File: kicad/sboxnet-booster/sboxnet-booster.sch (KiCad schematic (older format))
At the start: 53 parts, among them J1 sboxnet-stecker_02x17, J2 Conn_01x02_Male, J3 Conn_01x02_Male, J4 Conn_01x02_Male, J5 Screw_Terminal_01x04, J6 Screw_Terminal_01x04, J7 Power von externen 15V/4A Net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, SW1 Öffner, U1 l6206

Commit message: update booster kicad
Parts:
- removed C4: 220n, Capacitor_THT:C_Axial_L3.8mm_D2.6mm_P7.50mm_Horizontal, symbol Device:C
- removed J2: Conn_01x02_Male, Connector_PinHeader_2.54mm:PinHeader_1x02_P2.54mm_Vertical, symbol Connector:Conn_01x02_Male
- removed R13: 0.25 / 2W, Resistor_THT:R_Axial_DIN0414_L11.9mm_D4.5mm_P20.32mm_Horizontal, symbol Device:R
- removed R14, R15: 10k, Resistor_THT:R_Axial_DIN0204_L3.6mm_D1.6mm_P7.62mm_Horizontal, symbol Device:R
- removed U1: l6206, sboxnet:POWERSO36, symbol sboxnet:l6206
- added U1: L6206PSO, Package_SO:HSOP-36-1EP_11.0x15.9mm_P0.65mm_SlugDown_ThermalVias, symbol sboxnet:L6206PSO
- C1, C2, C3, C5, C6: footprint Capacitor_THT:C_Axial_L3.8mm_D2.6mm_P7.50mm_Horizontal -> Capacitor_SMD:C_1206_3216Metric
- C7: footprint Capacitor_THT:CP_Radial_D10.0mm_P2.50mm -> Capacitor_THT:CP_Radial_D12.5mm_P5.00mm
- C8: footprint Capacitor_THT:CP_Radial_D10.0mm_P2.50mm -> Capacitor_THT:CP_Radial_D5.0mm_P2.00mm
- R1, R10, R11, R2, R3, R4, R5, R6, R7, R8, R9: footprint Resistor_THT:R_Axial_DIN0204_L3.6mm_D1.6mm_P5.08mm_Horizontal -> Resistor_SMD:R_1206_3216Metric
- R12: value 0.25 / 2W -> 10k; footprint Resistor_THT:R_Axial_DIN0414_L11.9mm_D4.5mm_P20.32mm_Horizontal -> Resistor_SMD:R_1206_3216Metric
- R16, R17, R18, R19, R20: footprint Resistor_THT:R_Axial_DIN0204_L3.6mm_D1.6mm_P7.62mm_Horizontal -> Resistor_SMD:R_1206_3216Metric
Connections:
- net labels added: OUT1a, OUT1b, OUT2a, OUT2b, VBOOT, VCP
- net labels removed: SENSE
- wire segments 111 -> 86
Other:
- note removed: "Strommessung"

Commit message: fixed booster L6206PSO
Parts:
- J1: symbol sboxnet:sboxnet-stecker_02x17 -> sboxnet-booster-rescue:sboxnet-stecker_02x17-sboxnet
- U1: symbol sboxnet:L6206PSO -> sboxnet-booster-rescue:L6206PSO-sboxnet
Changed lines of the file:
@@
 	6485 3170 6530 3170
 $Comp
-L sboxnet:sboxnet-stecker_02x17 J1
+L sboxnet-booster-rescue:sboxnet-stecker_02x17-sboxnet J1
 U 1 1 5DC2D77D
 P 1200 3790
@@
 	730  3790 950  3790
 $Comp
-L sboxnet:L6206PSO U1
+L sboxnet-booster-rescue:L6206PSO-sboxnet U1
 U 1 1 5F0CD7F1
 P 5010 3755

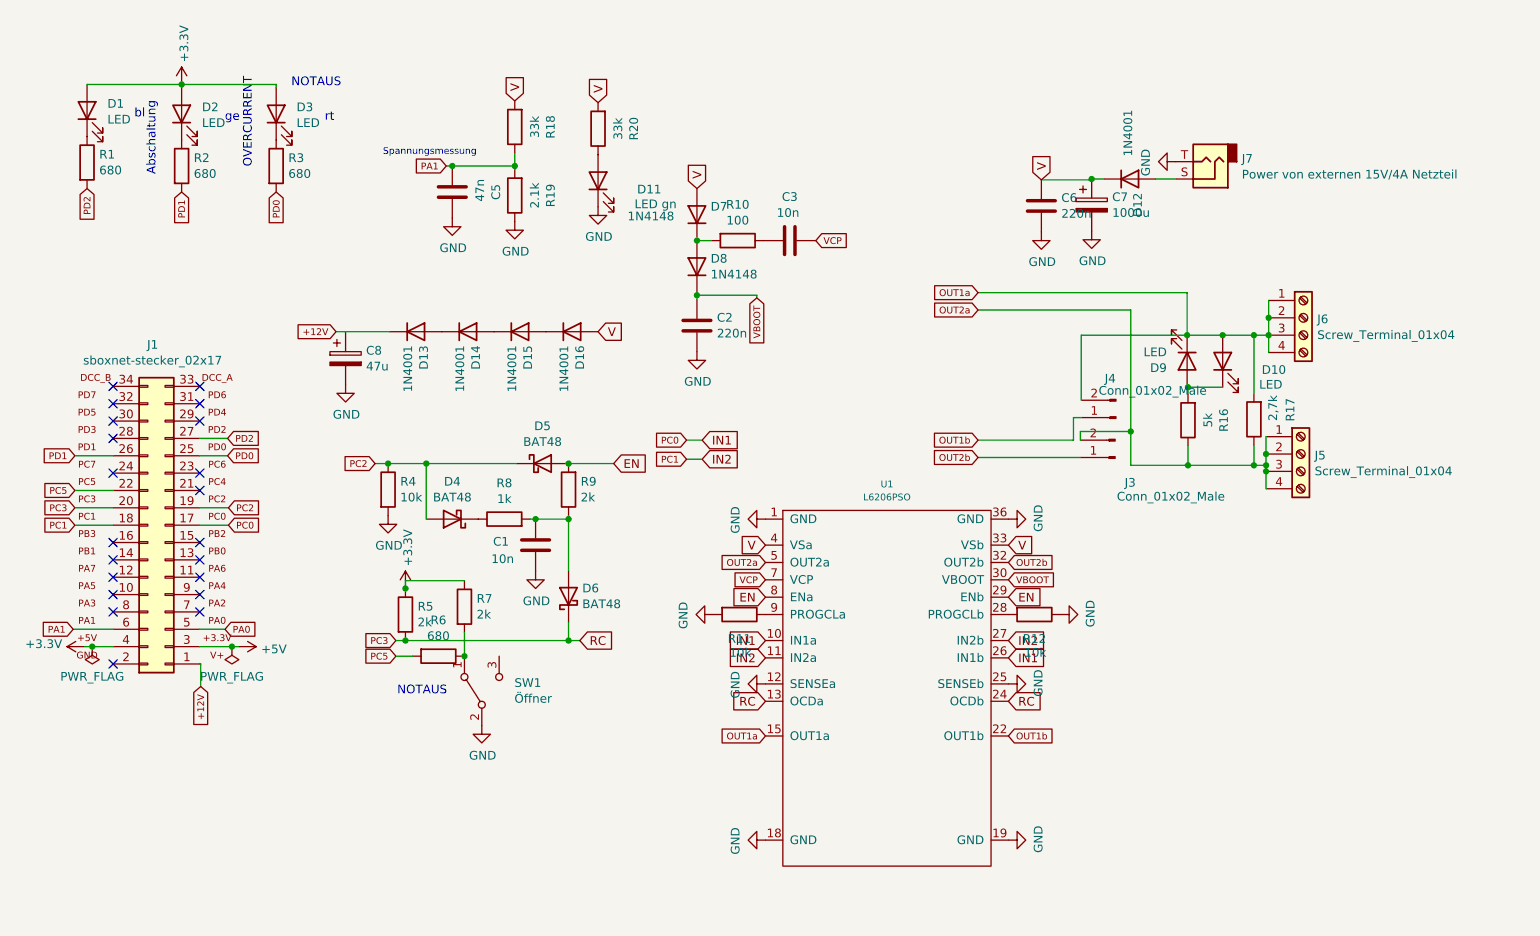
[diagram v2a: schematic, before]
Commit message: update booster layout with POWERSO Slug Down Terminal Vias
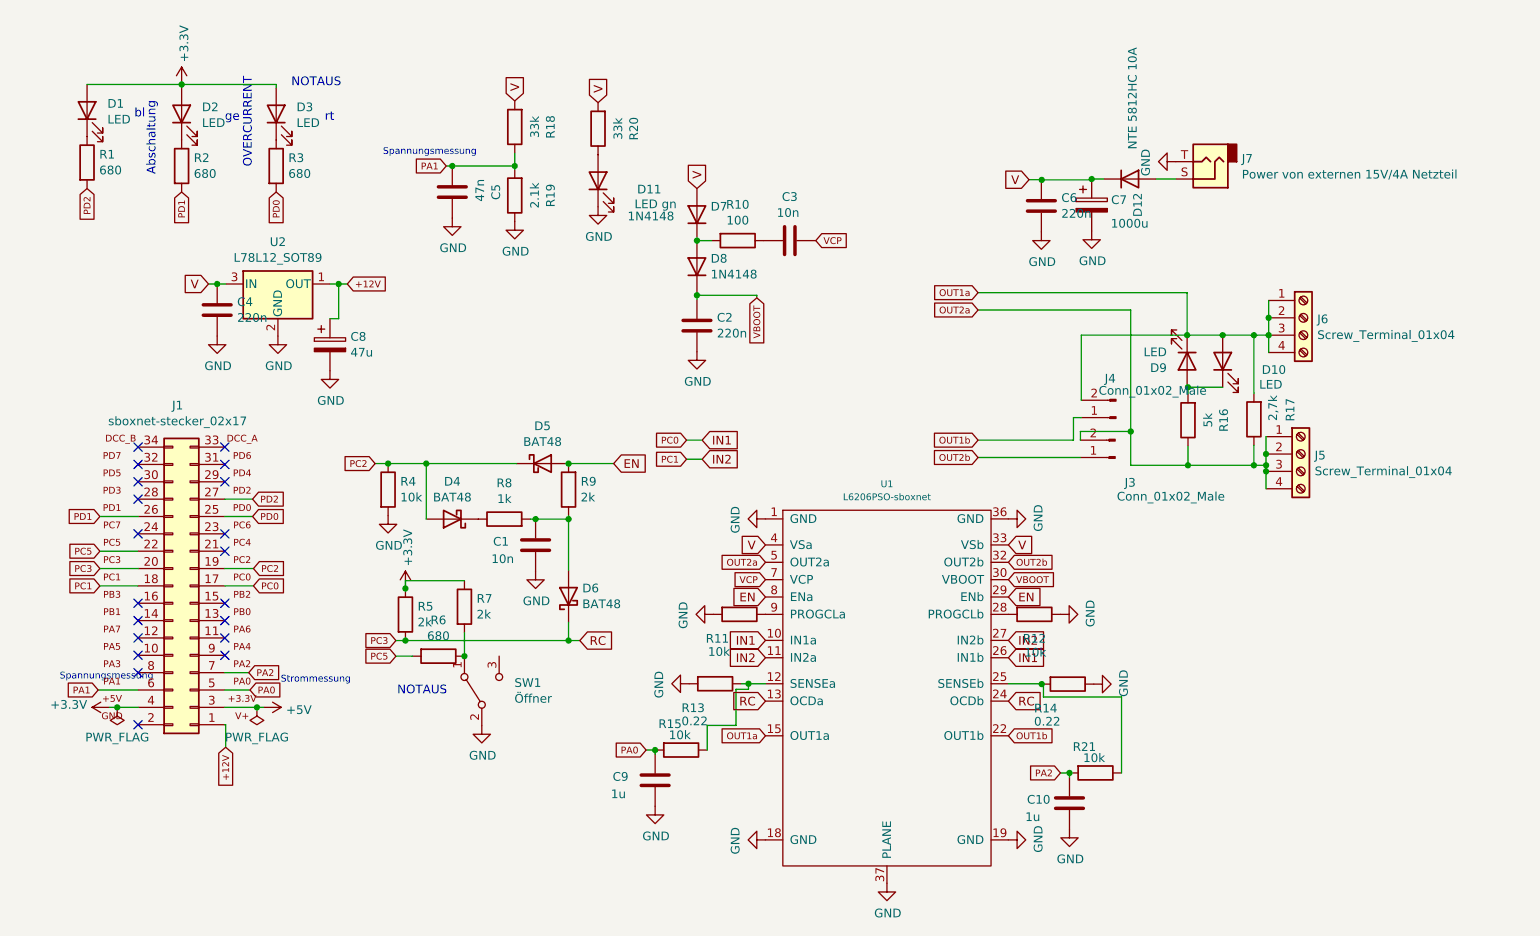
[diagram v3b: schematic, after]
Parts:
- removed D13, D14, D15, D16: 1N4001, Diode_THT:D_5W_P10.16mm_Horizontal, symbol Device:D
- removed U1: L6206PSO, Package_SO:HSOP-36-1EP_11.0x15.9mm_P0.65mm_SlugDown_ThermalVias, symbol sboxnet-booster-rescue:L6206PSO-sboxnet
- added C10, C9: 1u, Capacitor_SMD:C_1206_3216Metric, symbol Device:C
- added C4: 220n, Capacitor_SMD:C_1206_3216Metric, symbol Device:C
- added R13, R14: 0.22, Resistor_THT:R_Axial_Power_L38.0mm_W9.0mm_P45.72mm, symbol Device:R
- added R15, R21: 10k, Resistor_SMD:R_1206_3216Metric, symbol Device:R
- added U1: L6206PSO-sboxnet, Package_SO:HSOP-36-1EP_11.0x15.9mm_P0.65mm_SlugDown_ThermalVias, symbol sboxnet:L6206PSO-sboxnet
- added U2: L78L12_SOT89, Package_TO_SOT_SMD:SOT-89-3, symbol Regulator_Linear:L78L12_SOT89
- D12: value 1N4001 -> NTE 5812HC 10A
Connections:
- net +12V: now also C8.1, U2.1 (OUT)
- net EN: now also U1.29 (ENb), U1.8 (ENa)
- net GND: now also C10.1, C4.1, C9.1, R13.2, R14.1, U1.1 (GND), U1.18 (GND), U1.19 (GND), U1.36 (GND), U1.37 (PLANE), U2.2 (GND)
- net IN1: now also U1.10 (IN1a), U1.26 (IN1b)
- net IN2: now also U1.11 (IN2a), U1.27 (IN2b)
- net OUT1a: now also U1.15 (OUT1a)
- net OUT1b: now also U1.22 (OUT1b)
- net OUT2a: now also U1.5 (OUT2a)
- net OUT2b: now also U1.32 (OUT2b)
- net PA0: now also C9.2, R15.2
- net PC3: now also U1.13 (OCDa), U1.24 (OCDb)
- net V: now also C4.2, U1.33 (VSb), U1.4 (VSa), U2.3 (IN)
- net VBOOT: now also U1.30 (VBOOT)
- net VCP: now also U1.7 (VCP)
- net PA2: now reaches J1.7 (Pin_7)
- net PA2: now also C10.2, R21.2
- net at R12.2: now also U1.28 (PROGCLb)
- net at R11.1: now also U1.9 (PROGCLa)
- new net: R13.1, R15.1, U1.12 (SENSEa)
- new net: R14.2, R21.1, U1.25 (SENSEb)
- no-connect marks 21 -> 20
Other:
- note added: "Strommessung"
- moved on the sheet: C8, J1

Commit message: fixed
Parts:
- removed D7, D8: 1N4148, Diode_THT:D_5W_P10.16mm_Horizontal, symbol Device:D
- removed J1: sboxnet-stecker_02x17, sboxnet:sboxnet-stecker-2x17, symbol sboxnet-booster-rescue:sboxnet-stecker_02x17-sboxnet
- added D7, D8: 1N4148WS, Diode_SMD:D_SOD-323, symbol Diode:1N4148WS
- added J1: sboxnet-stecker_02x17, sboxnet:sboxnet-stecker-2x17, symbol sboxnet:sboxnet-stecker_02x17
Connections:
- net +12V: now also J1.1 (Pin_1)
- net +3V3: now also J1.3 (Pin_3)
- net +5V: now also J1.4 (Pin_4)
- net GND: now also J1.2 (Pin_2)
- net IN1: now also J1.17 (Pin_17)
- net IN2: now also J1.18 (Pin_18)
- net PA0: now also J1.5 (Pin_5)
- net PA1: now also J1.6 (Pin_6)
- net PA2: now also J1.7 (Pin_7)
- net PC2: now also J1.19 (Pin_19)
- net PC3: now also J1.20 (Pin_20)
- net PC5: now also J1.22 (Pin_22)
- net PD0: now also J1.25 (Pin_25)
- net PD1: now also J1.26 (Pin_26)
- net PD2: now also J1.27 (Pin_27)
- net V: now also D7.2 (A)
- net VBOOT: now also D8.1 (K)
- net at R10.2: now also D7.1 (K), D8.2 (A)
- no-connect marks 20 -> 19
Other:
- note added: "Spannungs\nmessung"
- moved on the sheet: C8
